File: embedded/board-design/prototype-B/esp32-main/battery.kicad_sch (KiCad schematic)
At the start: 14 parts, among them J7 Conn_01x03_Socket, Q5 FDN340P, Q6 FDN340P, U5 LTC4054ES5-4.2

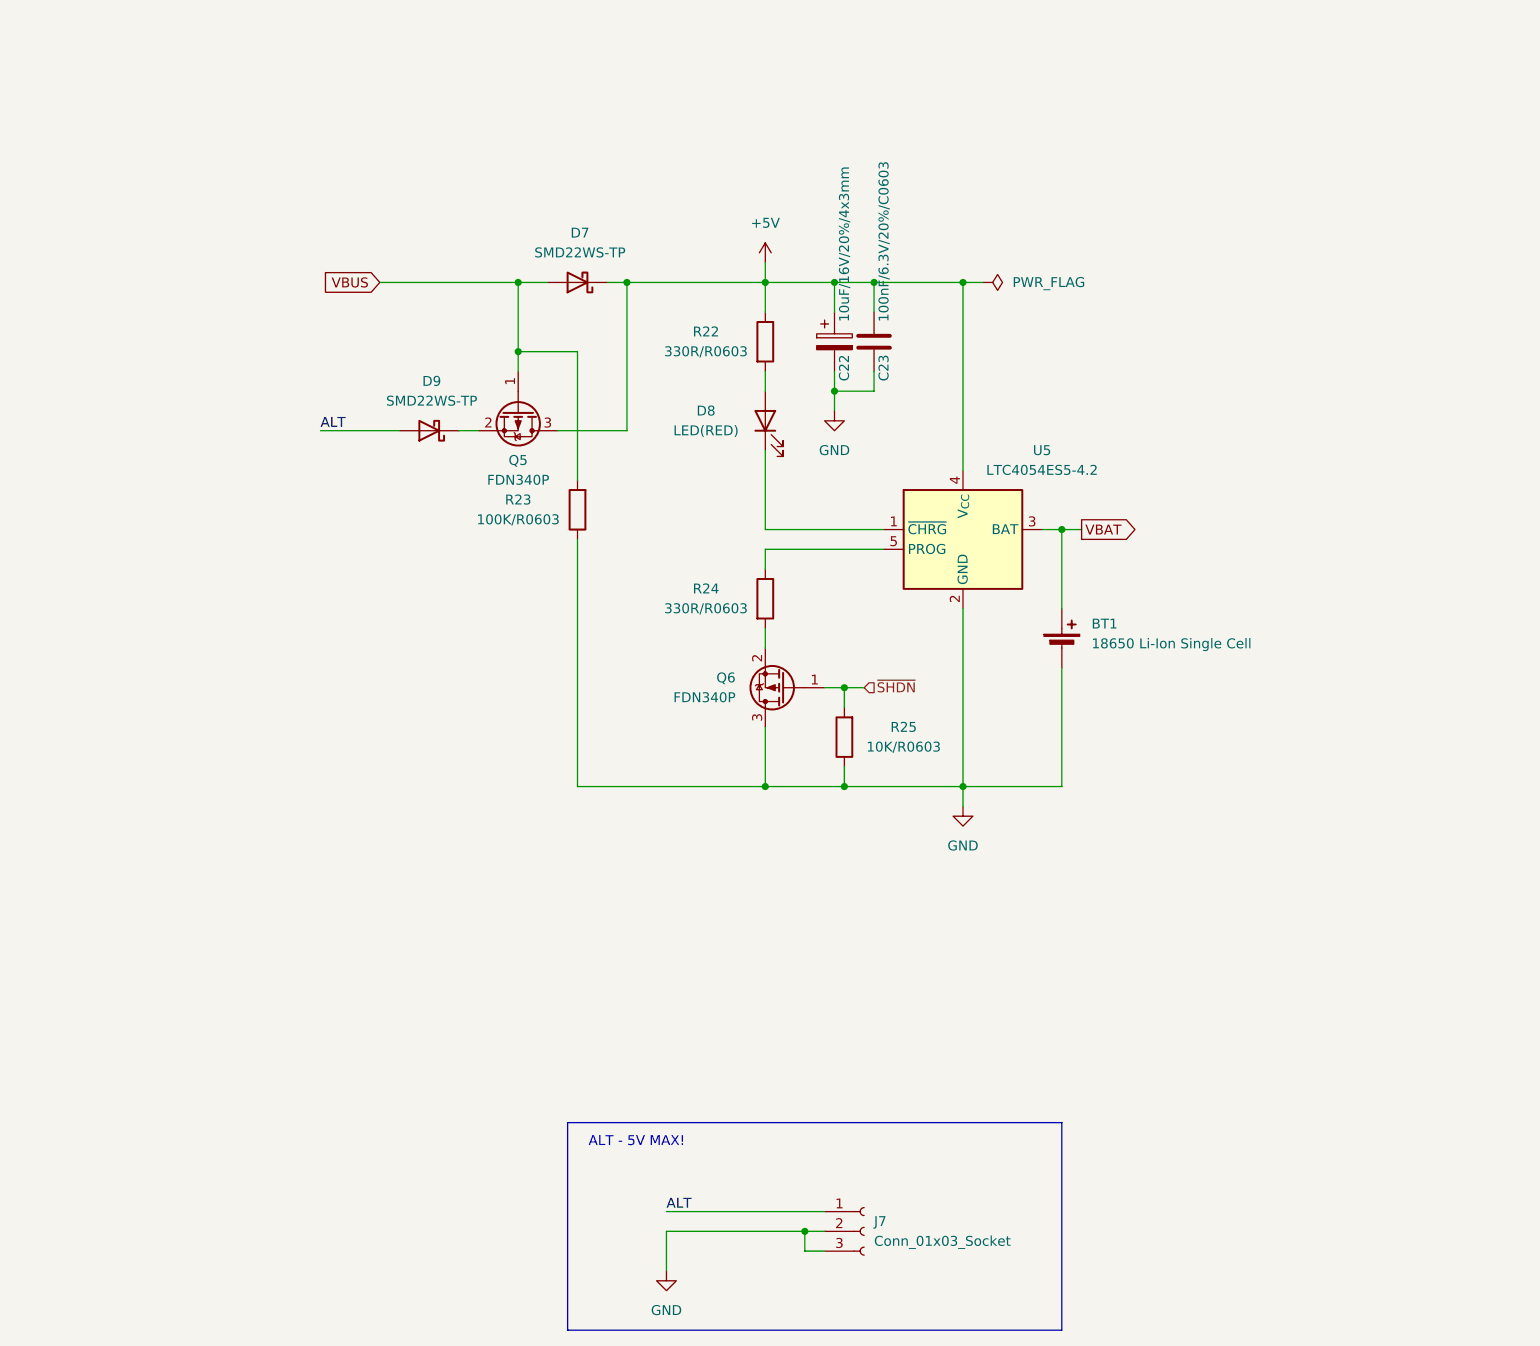
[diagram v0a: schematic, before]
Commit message: [prototype-B]
Refactored board size and battery switch design. Updated 3D model,
gerber and drill files, and BOM.

Signed-off-by: Nicolae-Andrei Vasile <vasilenicolaeandrei@gmail.com>
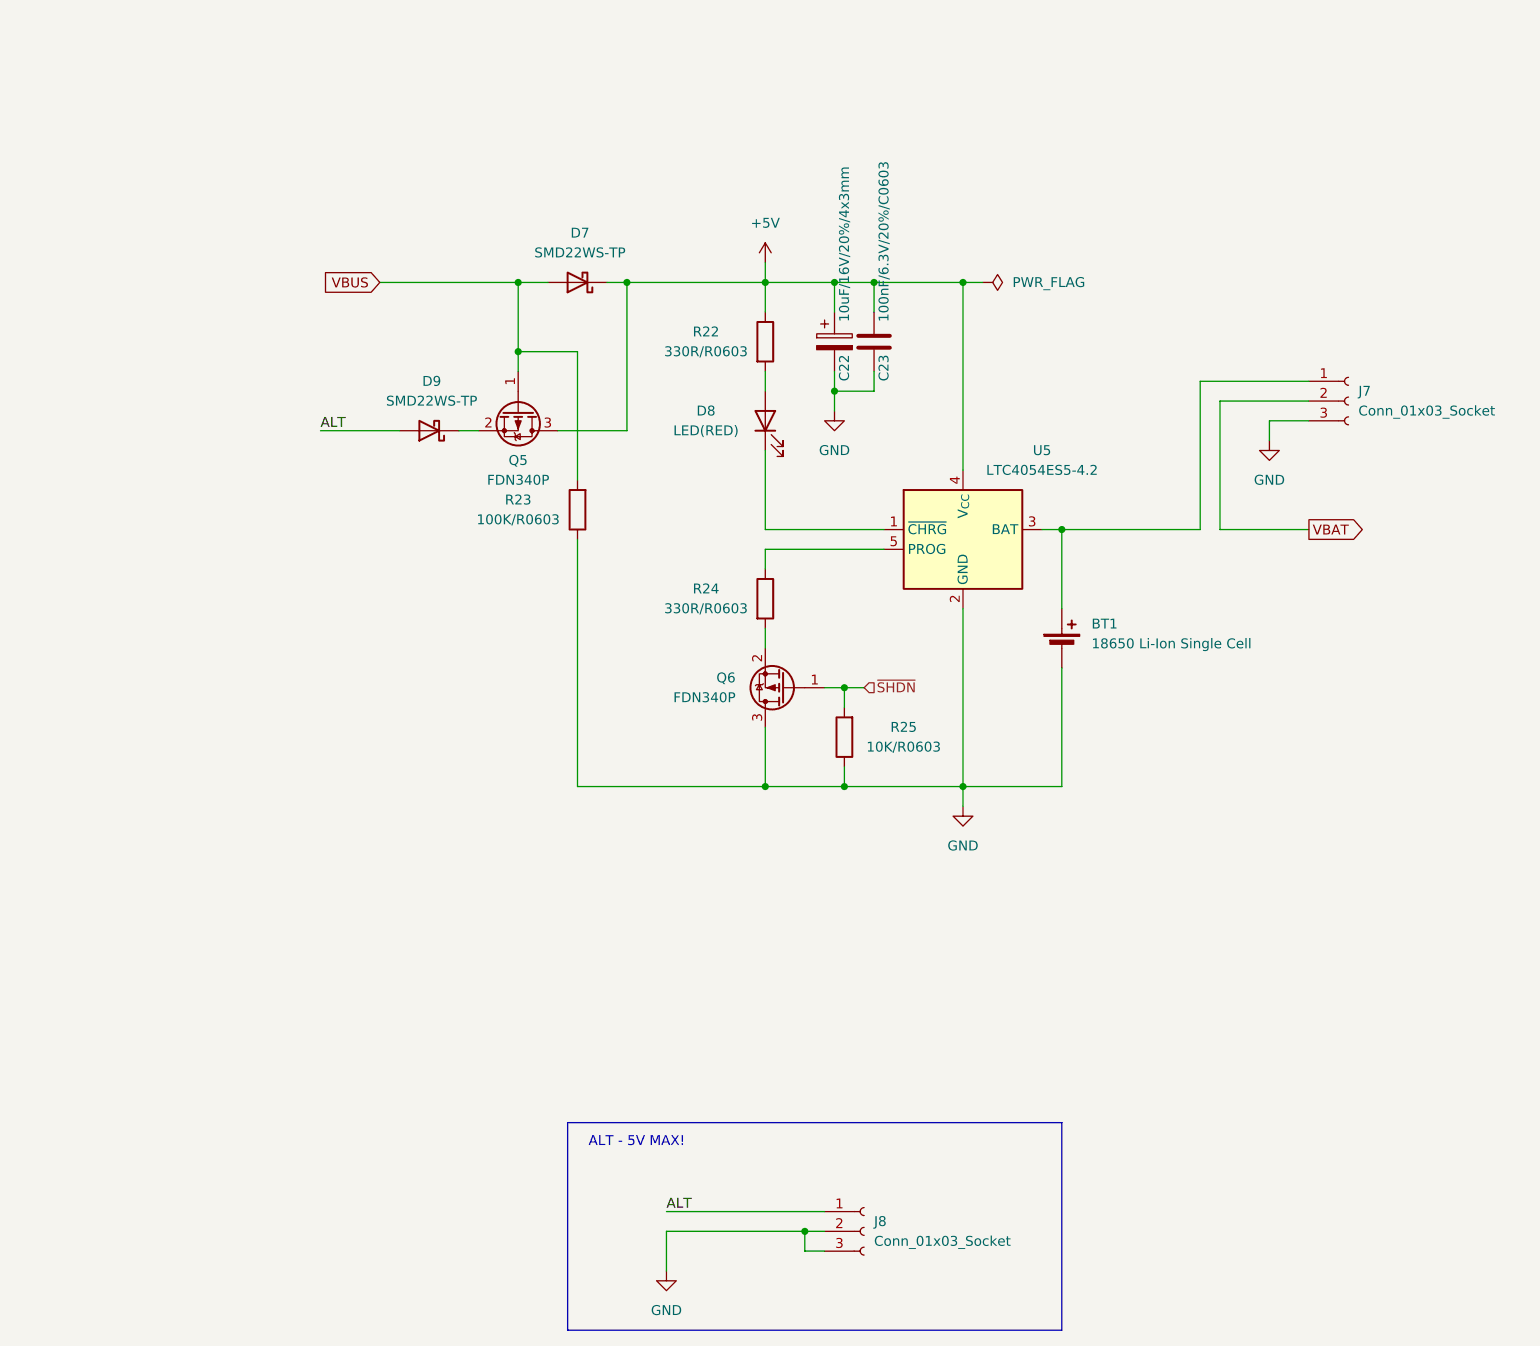
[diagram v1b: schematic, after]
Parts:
- added J8: Conn_01x03_Socket, Connector_Phoenix_MC:PhoenixContact_MC_1,5_3-G-3.81_1x03_P3.81mm_Horizontal, symbol Connector:Conn_01x03_Socket
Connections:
- net ALT: now also J8.1 (Pin_1); no longer J7.1 (Pin_1)
- net GND: now also J8.2 (Pin_2), J8.3 (Pin_3); no longer J7.2 (Pin_2)
- net VBAT: now also J7.2 (Pin_2); no longer BT1.1 (+), U5.3 (BAT)
- new net: BT1.1 (+), J7.1 (Pin_1), U5.3 (BAT)

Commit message: [prototype-B]
Updated prototype-B README.md. Refactored schematic.

Signed-off-by: Nicolae-Andrei Vasile <vasilenicolaeandrei@gmail.com>
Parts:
- removed J7: Conn_01x03_Socket, Connector_Phoenix_MC:PhoenixContact_MC_1,5_3-G-3.81_1x03_P3.81mm_Horizontal, symbol Connector:Conn_01x03_Socket
- renumbered D8 to D10, D9 to D11, D7 to D9
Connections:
- net VBAT: now also BT1.1 (+), U5.3 (BAT)
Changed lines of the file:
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@@
 	(wire
 		(pts
-			(xy 171.45 90.17) (xy 189.23 90.17)
+			(xy 171.45 90.17) (xy 190.5 90.17)
 		)
 		(stroke
@@
 	(wire
 		(pts
-			(xy 191.77 90.17) (xy 203.2 90.17)
-		)
-		(stroke
-			(width 0)
-			(type default)
-		)
-	)
-	(wire
-		(pts
 			(xy 158.75 123.19) (xy 171.45 123.19)
 		)
@@
 	(wire
 		(pts
-			(xy 191.77 73.66) (xy 191.77 90.17)
-		)
-		(stroke
-			(width 0)
-			(type default)
-		)
-	)
-	(wire
-		(pts
 			(xy 120.65 180.34) (xy 120.65 185.42)
 		)
@@
 	(wire
 		(pts
-			(xy 191.77 73.66) (xy 203.2 73.66)
-		)
-		(stroke
-			(width 0)
-			(type default)
-		)
-	)
-	(wire
-		(pts
 			(xy 143.51 110.49) (xy 146.05 110.49)
 		)
@@
 	(wire
 		(pts
-			(xy 189.23 71.12) (xy 189.23 90.17)
-		)
-		(stroke
-			(width 0)
-			(type default)
-		)
-	)
-	(wire
-		(pts
 			(xy 171.45 100.33) (xy 171.45 90.17)
 		)
@@
 	(wire
 		(pts
-			(xy 198.12 76.2) (xy 198.12 78.74)
-		)
-		(stroke
-			(width 0)
-			(type default)
-		)
-	)
-	(wire
-		(pts
 			(xy 147.32 72.39) (xy 147.32 69.85)
 		)
@@
 		(pts
 			(xy 143.51 120.65) (xy 143.51 123.19)
-		)
-		(stroke
-			(width 0)
-			(type default)
-		)
-	)
-	(wire
-		(pts
-			(xy 203.2 76.2) (xy 198.12 76.2)
-		)
-		(stroke
-			(width 0)
-			(type default)
-		)
-	)
-	(wire
-		(pts
-			(xy 189.23 71.12) (xy 203.2 71.12)
 		)
 		(stroke
@@
 	(global_label "VBAT"
 		(shape output)
-		(at 203.2 90.17 0)
+		(at 190.5 90.17 0)
 		(fields_autoplaced yes)
 		(effects
@@
 		)
 		(property "Intersheetrefs" "${INTERSHEET_REFS}"
-			(at 210.6 90.17 0)
+			(at 197.9 90.17 0)
 			(effects
 				(font
@@
 		(on_board yes)
 		(dnp no)
-		(property "Reference" "D7"
+		(property "Reference" "D9"
 			(at 109.5375 52.07 0)
 			(effects
@@
 			(project "esp32-main"
 				(path "/6d02e045-d1b3-4320-a4f8-f5e2c734acd4/9cfdfa29-fef4-49c3-96a5-094ec94d9453"
-					(reference "D7")
+					(reference "D9")
 					(unit 1)
 				)
@@
 				(path "/6d02e045-d1b3-4320-a4f8-f5e2c734acd4/9cfdfa29-fef4-49c3-96a5-094ec94d9453"
 					(reference "R23")
-					(unit 1)
-				)
-			)
-		)
-	)
-	(symbol
-		(lib_id "power:GND")
-		(at 198.12 78.74 0)
-		(unit 1)
-		(exclude_from_sim no)
-		(in_bom yes)
-		(on_board yes)
-		(dnp no)
-		(fields_autoplaced yes)
-		(property "Reference" "#PWR026"
-			(at 198.12 85.09 0)
-			(effects
-				(font
-					(size 1.27 1.27)
-				)
-				(hide yes)
-			)
-		)
-		(property "Value" "GND"
-			(at 198.12 83.82 0)
-			(effects
-				(font
-					(size 1.27 1.27)
-				)
-			)
-		)
-		(property "Footprint" ""
-			(at 198.12 78.74 0)
-			(effects
-				(font
-					(size 1.27 1.27)
-				)
-				(hide yes)
-			)
-		)
-		(property "Datasheet" ""
-			(at 198.12 78.74 0)
-			(effects
-				(font
-					(size 1.27 1.27)
-				)
-				(hide yes)
-			)
-		)
-		(property "Description" "Power symbol creates a global label with name \"GND\" , ground"
-			(at 198.12 78.74 0)
-			(effects
-				(font
-					(size 1.27 1.27)
-				)
-				(hide yes)
-			)
-		)
-		(pin "1"
-		)
-		(instances
-			(project "esp32-main"
-				(path "/6d02e045-d1b3-4320-a4f8-f5e2c734acd4/9cfdfa29-fef4-49c3-96a5-094ec94d9453"
-					(reference "#PWR026")
 					(unit 1)
 				)
@@
 		(dnp no)
 		(fields_autoplaced yes)
-		(property "Reference" "#PWR027"
+		(property "Reference" "#PWR026"
 			(at 158.75 132.08 0)
 			(effects
@@
 			(project "esp32-main"
 				(path "/6d02e045-d1b3-4320-a4f8-f5e2c734acd4/9cfdfa29-fef4-49c3-96a5-094ec94d9453"
-					(reference "#PWR027")
+					(reference "#PWR026")
 					(unit 1)
 				)
@@
 		(dnp no)
 		(fields_autoplaced yes)
-		(property "Reference" "#PWR028"
+		(property "Reference" "#PWR027"
 			(at 120.65 191.77 0)
 			(effects
@@
 			(project "esp32-main"
 				(path "/6d02e045-d1b3-4320-a4f8-f5e2c734acd4/9cfdfa29-fef4-49c3-96a5-094ec94d9453"
-					(reference "#PWR028")
+					(reference "#PWR027")
 					(unit 1)
 				)
@@
 		(on_board yes)
 		(dnp no)
-		(property "Reference" "D9"
+		(property "Reference" "D11"
 			(at 90.4875 71.12 0)
 			(effects
@@
 			(project "esp32-main"
 				(path "/6d02e045-d1b3-4320-a4f8-f5e2c734acd4/9cfdfa29-fef4-49c3-96a5-094ec94d9453"
-					(reference "D9")
+					(reference "D11")
 					(unit 1)
 				)
@@
 		(dnp no)
 		(fields_autoplaced yes)
-		(property "Reference" "#FLG04"
+		(property "Reference" "#FLG06"
 			(at 163.195 58.42 0)
 			(effects
@@
 			(project ""
 				(path "/6d02e045-d1b3-4320-a4f8-f5e2c734acd4/9cfdfa29-fef4-49c3-96a5-094ec94d9453"
-					(reference "#FLG04")
+					(reference "#FLG06")
 					(unit 1)
 				)
@@
 				(path "/6d02e045-d1b3-4320-a4f8-f5e2c734acd4/9cfdfa29-fef4-49c3-96a5-094ec94d9453"
 					(reference "C22")
-					(unit 1)
-				)
-			)
-		)
-	)
-	(symbol
-		(lib_id "Connector:Conn_01x03_Socket")
-		(at 208.28 73.66 0)
-		(unit 1)
-		(exclude_from_sim no)
-		(in_bom yes)
-		(on_board yes)
-		(dnp no)
-		(property "Reference" "J7"
-			(at 209.55 72.3899 0)
-			(effects
-				(font
-					(size 1.27 1.27)
-				)
-				(justify left)
-			)
-		)
-		(property "Value" "Conn_01x03_Socket"
-			(at 209.55 74.93 0)
-			(effects
-				(font
-					(size 1.27 1.27)
-				)
-				(justify left)
-			)
-		)
-		(property "Footprint" "Connector_Phoenix_MC:PhoenixContact_MC_1,5_3-G-3.81_1x03_P3.81mm_Horizontal"
-			(at 208.28 73.66 0)
-			(effects
-				(font
-					(size 1.27 1.27)
-				)
-				(hide yes)
-			)
-		)
-		(property "Datasheet" "~"
-			(at 208.28 73.66 0)
-			(effects
-				(font
-					(size 1.27 1.27)
-				)
-				(hide yes)
-			)
-		)
-		(property "Description" "Generic connector, single row, 01x03, script generated"
-			(at 208.28 73.66 0)
-			(effects
-				(font
-					(size 1.27 1.27)
-				)
-				(hide yes)
-			)
-		)
-		(pin "1"
-		)
-		(pin "2"
-		)
-		(pin "3"
-		)
-		(instances
-			(project "esp32-main"
-				(path "/6d02e045-d1b3-4320-a4f8-f5e2c734acd4/9cfdfa29-fef4-49c3-96a5-094ec94d9453"
-					(reference "J7")
 					(unit 1)
 				)
@@
 		(on_board yes)
 		(dnp no)
-		(property "Reference" "D8"
+		(property "Reference" "D10"
 			(at 125.73 74.93 90)
 			(effects
@@
 			(project "esp32-main"
 				(path "/6d02e045-d1b3-4320-a4f8-f5e2c734acd4/9cfdfa29-fef4-49c3-96a5-094ec94d9453"
-					(reference "D8")
+					(reference "D10")
 					(unit 1)
 				)
